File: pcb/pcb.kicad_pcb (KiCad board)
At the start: 2 copper layers, 109 x 54 mm, 60 parts, among them J1 MALE, J10 TC2030_NL, J101 MALE, J102 FEMALE, J103 MALE, J104 FEMALE, J105 MALE, J106 FEMALE, J107 MALE, J108 FEMALE, J11 STANDOFF, J111 STANDOFF, J112 STANDOFF, J113 STANDOFF, J114 STANDOFF, J12 STANDOFF, J13 STANDOFF, J14 STANDOFF, J2 FEMALE, J3 MALE, J4 FEMALE, J5 MALE, J6 FEMALE, J7 MALE, J8 FEMALE, J9 DTR, Q1 2N3904, SW1 ACTION, SW2 ACTION, SW3 ACTION, SW4 ACTION, U3 ATmega328P-MU, Y1 YSX321SL

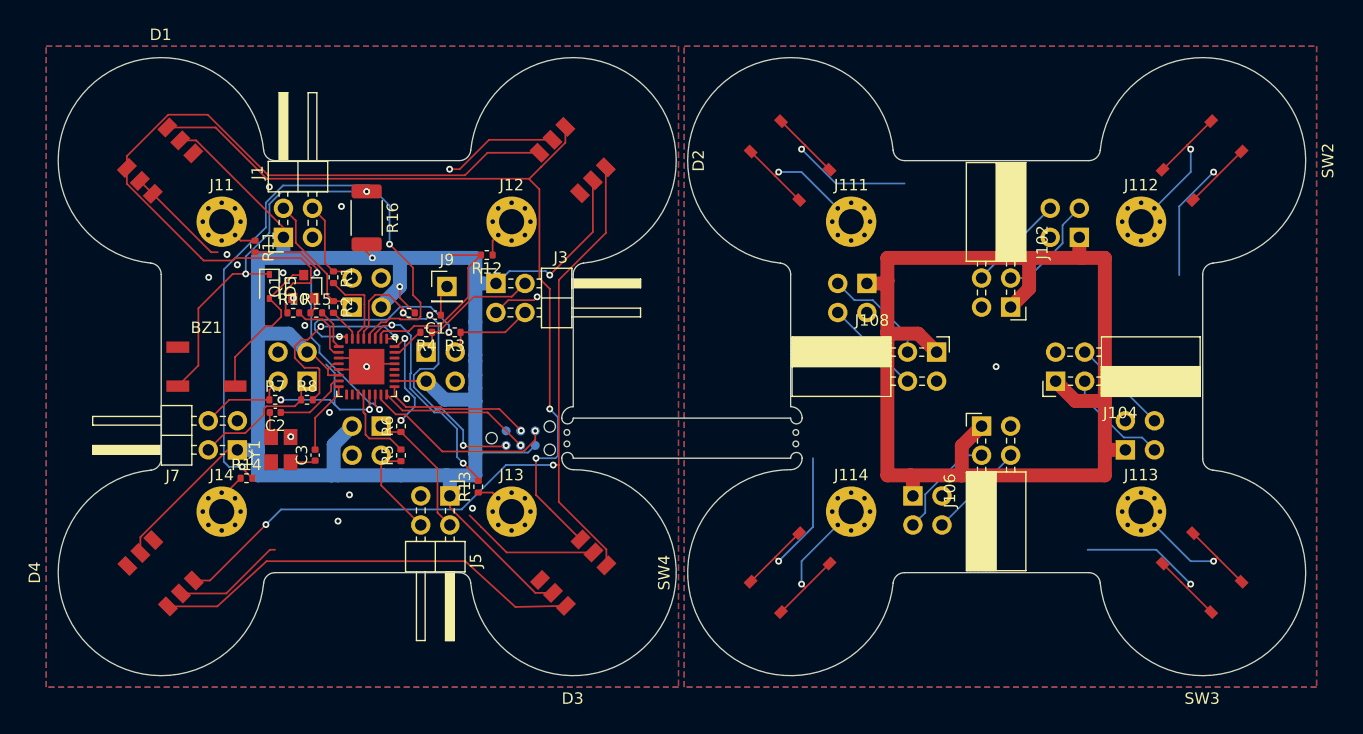
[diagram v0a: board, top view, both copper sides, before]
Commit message: Swap sides to move mouse bites in safer position
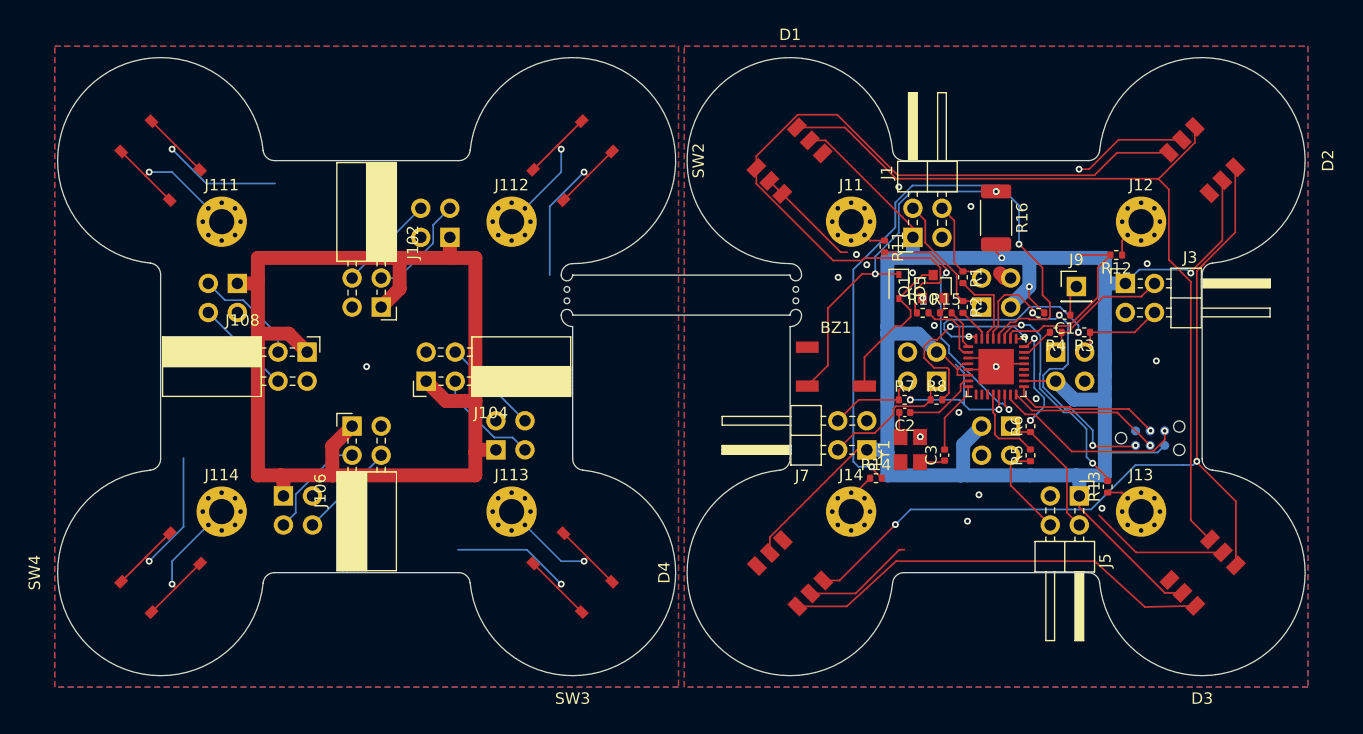
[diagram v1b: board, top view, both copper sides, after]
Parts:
- removed the mouse-bite at (158.5, 111.2)
- removed the mouse-bite at (138.5, 111.2)
- added mouse-bite: VAL**, node:mouse-bite, F.Cu at (138.5, 98.8)
- added mouse-bite: VAL**, node:mouse-bite, F.Cu at (158.5, 98.8)
- moved C2 55.0 mm to (168.0, 109.0)
- moved J102 55.0 mm to (122.3, 99.8)
- moved J107 55.0 mm to (109.7, 97.7)
- moved J108 55.0 mm to (115.8, 103.7)
- moved J6 55.0 mm to (177.3, 110.2)
- moved J7 55.0 mm to (164.7, 112.3)
- moved J8 55.0 mm to (170.8, 106.3)
- moved R4 55.0 mm to (181.2, 102.0)
- moved BZ1 55.0 mm to (162.0, 105.0)
- moved C1 55.0 mm to (182.0, 100.5)
- moved C3 55.0 mm to (171.5, 112.7)
- moved D1 55.0 mm to (158.0, 87.0)
- moved D2 55.0 mm to (194.0, 87.0)
- moved D3 55.0 mm to (194.0, 123.0)
- moved D4 55.0 mm to (158.0, 123.0)
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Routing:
- net GNDB: track 53.4 -> 50.3 mm, vias 17 -> 18
- net Net-(D1-Pad3): track 75.3 -> 72.7 mm, vias 2 -> 0
- net Net-(D2-Pad3): track 74.3 -> 75.1 mm
- net +5VB: track 177.1 -> 177.7 mm
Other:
- outline, holes or cut-outs redrawn

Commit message: Fix DRC errors
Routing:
- net GNDB: track 50.3 -> 51.6 mm, vias 18 -> 19
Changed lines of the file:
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@@
     (thickness 1)
     (drawings 70)
-    (tracks 575)
+    (tracks 577)
     (zones 0)
     (modules 60)
@@
     (36 B.SilkS user hide)
     (37 F.SilkS user hide)
-    (38 B.Mask user hide)
+    (38 B.Mask user)
     (39 F.Mask user hide)
     (40 Dwgs.User user hide)
@@
     (44 Edge.Cuts user)
     (45 Margin user hide)
-    (46 B.CrtYd user hide)
-    (47 F.CrtYd user hide)
+    (46 B.CrtYd user)
+    (47 F.CrtYd user)
     (48 B.Fab user hide)
     (49 F.Fab user hide)
   )
   (setup
-    (last_trace_width 0.1524)
+    (last_trace_width 0.508)
     (user_trace_width 0.1524)
+    (user_trace_width 0.508)
     (user_trace_width 1.2192)
     (trace_clearance 0.1524)
@@
   (gr_arc (start 138.5 97) (end 138 97) (angle -180) (layer Edge.Cuts) (width 0.05))
   (gr_arc (start 139 97) (end 139 96) (angle -90) (layer Edge.Cuts) (width 0.05))
-  (gr_line (start 181.5 89) (end 181.5 94) (layer B.Mask) (width 0.15))
-  (gr_line (start 186.5 89) (end 181.5 89) (layer B.Mask) (width 0.15))
-  (gr_line (start 186.5 94) (end 186.5 89) (layer B.Mask) (width 0.15))
-  (gr_line (start 181.5 94) (end 186.5 94) (layer B.Mask) (width 0.15))
-  (gr_line (start 184 91.5) (end 186 89.5) (layer B.Mask) (width 0.15))
-  (gr_line (start 184 91.5) (end 186 93.5) (layer B.Mask) (width 0.15))
-  (gr_line (start 184 93.500001) (end 184 89.499999) (layer B.Mask) (width 0.15))
-  (gr_line (start 183 93.5) (end 183 89.5) (layer B.Mask) (width 0.15))
-  (gr_line (start 183 89.5) (end 184 89.499999) (layer B.Mask) (width 0.15))
-  (gr_line (start 181.999999 91.5) (end 184 91.5) (layer B.Mask) (width 0.15))
-  (gr_line (start 182 93.5) (end 184 93.500001) (layer B.Mask) (width 0.15))
-  (gr_line (start 182 93.5) (end 182 89.5) (layer B.Mask) (width 0.15))
+  (gr_line (start 179.5 87.5) (end 179.5 92.5) (layer B.Mask) (width 0.15))
+  (gr_line (start 184.5 87.5) (end 179.5 87.5) (layer B.Mask) (width 0.15))
+  (gr_line (start 184.5 92.5) (end 184.5 87.5) (layer B.Mask) (width 0.15))
+  (gr_line (start 179.5 92.5) (end 184.5 92.5) (layer B.Mask) (width 0.15))
+  (gr_line (start 182 90) (end 184 88) (layer B.Mask) (width 0.15))
+  (gr_line (start 182 90) (end 184 92) (layer B.Mask) (width 0.15))
+  (gr_line (start 182 92.000001) (end 182 87.999999) (layer B.Mask) (width 0.15))
+  (gr_line (start 181 92) (end 181 88) (layer B.Mask) (width 0.15))
+  (gr_line (start 181 88) (end 182 87.999999) (layer B.Mask) (width 0.15))
+  (gr_line (start 179.999999 90) (end 182 90) (layer B.Mask) (width 0.15))
+  (gr_line (start 180 92) (end 182 92.000001) (layer B.Mask) (width 0.15))
+  (gr_line (start 180 92) (end 180 88) (layer B.Mask) (width 0.15))
   (gr_line (start 115 111) (end 117 111) (layer F.Mask) (width 0.15))
   (gr_line (start 115 109) (end 115 111) (layer F.Mask) (width 0.15))
@@
   (via (at 185.25 117.375) (size 0.6) (drill 0.3) (layers F.Cu B.Cu) (net 34))
   (via (at 173.5 118.5) (size 0.6) (drill 0.3) (layers F.Cu B.Cu) (net 34))
-  (via (at 183.25 87.75) (size 0.6) (drill 0.3) (layers F.Cu B.Cu) (net 34))
-  (segment (start 184.128711 87.75) (end 183.25 87.75) (width 0.1524) (layer F.Cu) (net 34))
-  (segment (start 186.696478 85.182233) (end 184.128711 87.75) (width 0.1524) (layer F.Cu) (net 34))
-  (segment (start 192.232233 85.182233) (end 186.696478 85.182233) (width 0.1524) (layer F.Cu) (net 34))
   (via (at 174.5 116.2) (size 0.6) (drill 0.3) (layers F.Cu B.Cu) (net 34))
   (via (at 162.2 97.2) (size 0.6) (drill 0.3) (layers F.Cu B.Cu) (net 34))
@@
   (via (at 179.5 107.8) (size 0.6) (drill 0.3) (layers F.Cu B.Cu) (net 34))
   (via (at 163.8 95.2) (size 0.6) (drill 0.3) (layers F.Cu B.Cu) (net 34))
-  (segment (start 176.76 97.26) (end 176.342001 96.842001) (width 1.2192) (layer F.Cu) (net 34))
-  (segment (start 177.27 97.26) (end 176.76 97.26) (width 1.2192) (layer F.Cu) (net 34))
   (via (at 190 104.5) (size 0.6) (drill 0.3) (layers F.Cu B.Cu) (net 34))
-  (via (at 189.2 96) (size 0.6) (drill 0.3) (layers F.Cu B.Cu) (net 34))
+  (via (at 188.9 95.6) (size 0.6) (drill 0.3) (layers F.Cu B.Cu) (net 34))
+  (segment (start 192.232233 85.182233) (end 186.696478 85.182233) (width 0.1524) (layer F.Cu) (net 34))
+  (segment (start 186.696478 85.182233) (end 184.128711 87.75) (width 0.1524) (layer F.Cu) (net 34))
+  (segment (start 184.128711 87.75) (end 183.25 87.75) (width 0.1524) (layer F.Cu) (net 34))
+  (via (at 185.5 93) (size 0.6) (drill 0.3) (layers F.Cu B.Cu) (net 34))
+  (segment (start 177.27 97.26) (end 176.86 97.26) (width 0.6096) (layer F.Cu) (net 34))
+  (segment (start 177.27 97.26) (end 176.96 97.26) (width 0.508) (layer F.Cu) (net 34))
+  (segment (start 176.96 97.26) (end 175.8 96.1) (width 0.508) (layer F.Cu) (net 34))
+  (via (at 170.3 87.4) (size 0.6) (drill 0.3) (layers F.Cu B.Cu) (net 34))
   (segment (start 187.01 93.99) (end 188.666 92.334) (width 0.1524) (layer F.Cu) (net 35))
   (segment (start 187.01 95.25) (end 187.01 93.99) (width 0.1524) (layer F.Cu) (net 35))

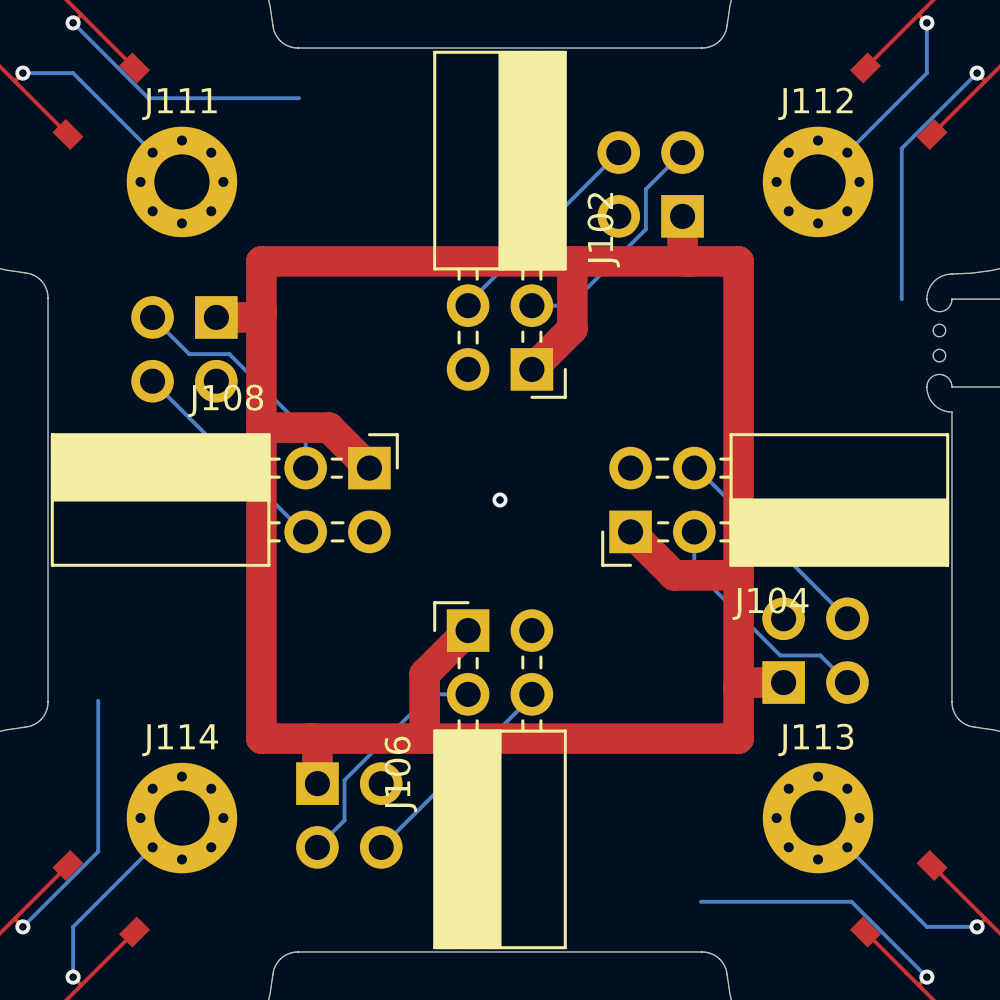
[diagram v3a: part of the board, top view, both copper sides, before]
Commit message: Retrace upper board
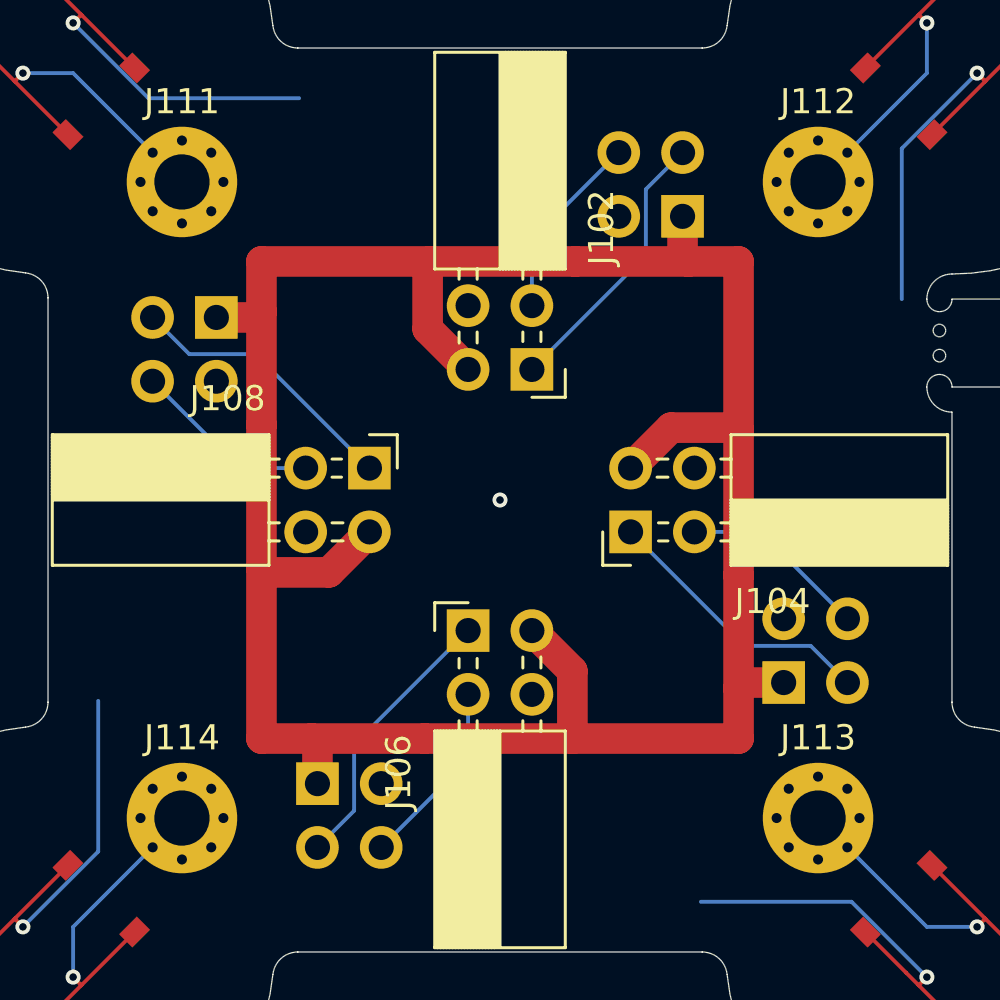
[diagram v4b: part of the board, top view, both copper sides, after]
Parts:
- R16: value 15 0.5W -> 22 0.5W
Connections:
- J102 pad 1: +5V -> Net-(J101-Pad2)
- J102 pad 2: Net-(J101-Pad2) -> Net-(J101-Pad4)
- J102 pad 3: GND -> +5V
- J102 pad 4: Net-(J101-Pad4) -> GND
- J104 pad 1: +5V -> Net-(J103-Pad2)
- J104 pad 2: Net-(J103-Pad2) -> Net-(J103-Pad4)
- J104 pad 3: GND -> +5V
- J104 pad 4: Net-(J103-Pad4) -> GND
- J106 pad 1: +5V -> Net-(J105-Pad2)
- J106 pad 2: Net-(J105-Pad2) -> Net-(J105-Pad4)
- J106 pad 3: GND -> +5V
- J106 pad 4: Net-(J105-Pad4) -> GND
- J108 pad 1: +5V -> Net-(J107-Pad2)
- J108 pad 2: Net-(J107-Pad2) -> Net-(J107-Pad4)
- J108 pad 3: GND -> +5V
- J108 pad 4: Net-(J107-Pad4) -> GND
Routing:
- net Net-(J103-Pad2): track 9.46 -> 11.1 mm
- net Net-(J107-Pad2): track 9.46 -> 11.1 mm
- net Net-(J101-Pad2): track 9.46 -> 11.1 mm
- net Net-(J105-Pad2): track 9.46 -> 11.1 mm
- net Net-(J103-Pad4): track 8.58 -> 7.53 mm
- net Net-(J107-Pad4): track 8.58 -> 7.53 mm
- net Net-(J105-Pad4): track 8.58 -> 7.53 mm
- net Net-(J101-Pad4): track 8.58 -> 7.53 mm
